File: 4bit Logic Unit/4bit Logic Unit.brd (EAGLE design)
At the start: 161.3 x 110.2 mm, 91 parts

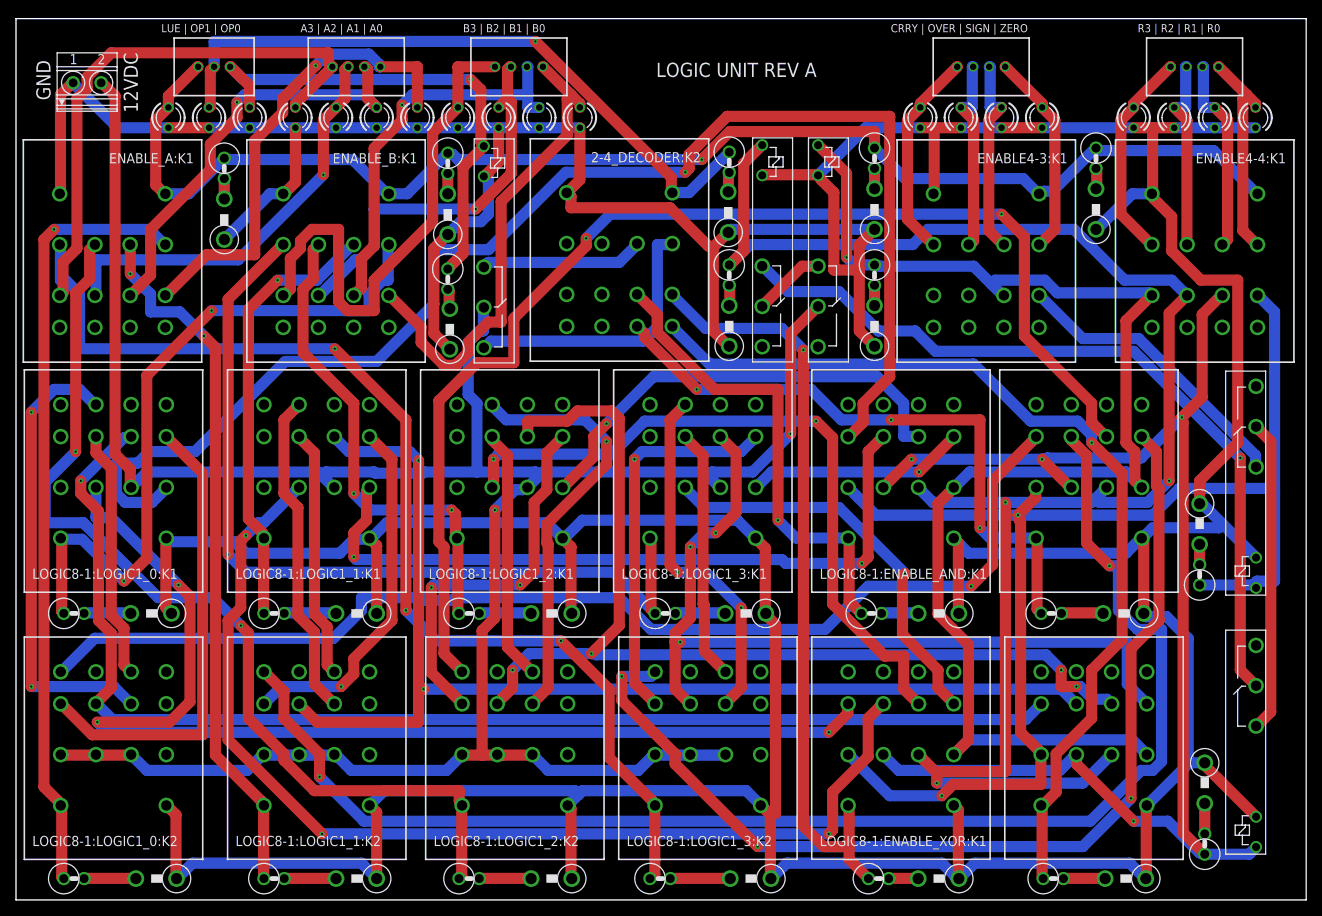
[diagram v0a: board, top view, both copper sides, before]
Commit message: Using updated connectors
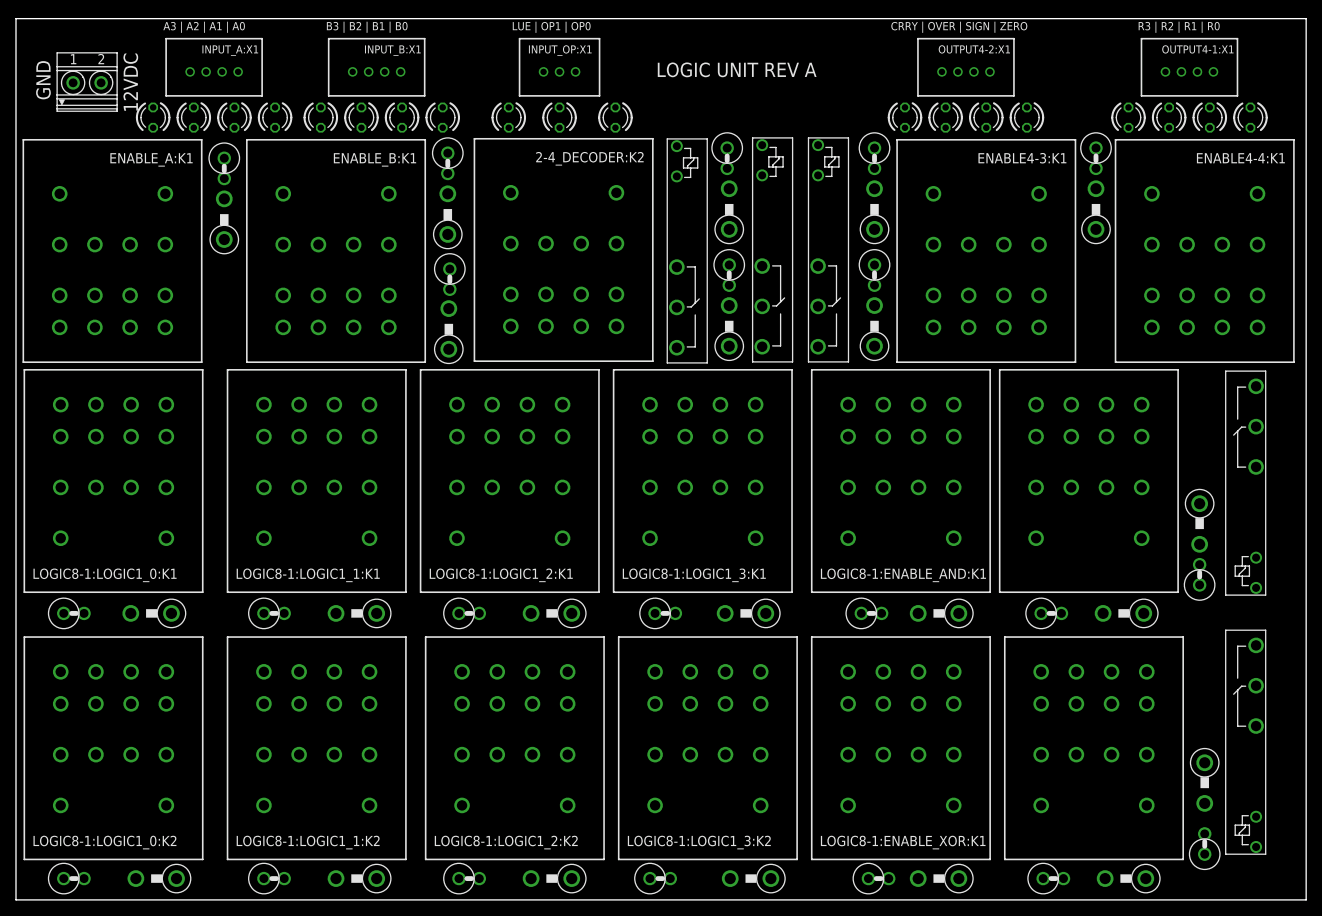
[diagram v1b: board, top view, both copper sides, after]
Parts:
- moved INPUT_OP:LED0 45.7 mm to (74.9, 96.5)
- moved INPUT_OP:LED1 43.8 mm to (67.9, 96.5)
- moved INPUT_OP:X1 43.2 mm to (67.9, 102.2), turned to 180 degrees
- moved INPUT_OP:LED2 42.5 mm to (61.6, 96.5)
- moved 2-4_DECODER:D1 38.1 mm to (88.9, 91.4)
- moved 2-4_DECODER:D2 38.0 mm to (89.2, 85.1)
- moved 2-4_DECODER:D4 37.9 mm to (54.1, 70.1)
- moved 2-4_DECODER:D3 37.9 mm to (54.2, 76.3)
- moved 2-4_DECODER:K1 24.1 mm to (81.4, 93.9)
- moved INPUT_A:X1 17.8 mm to (24.8, 102.2)
- moved INPUT_B:X1 17.8 mm to (45.1, 102.2)
- moved INPUT_A:LED0 17.8 mm to (32.4, 96.5)
- moved INPUT_A:LED1 17.8 mm to (27.3, 96.5)
- moved INPUT_A:LED2 17.8 mm to (22.2, 96.5)
- moved INPUT_A:LED3 17.8 mm to (17.1, 96.5)
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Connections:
- net CARRY: now also OUTPUT4-2:X1.1; no longer OUTPUT4-2:X1.4
- net N$1: now also INPUT_A:X1.4; no longer INPUT_A:X1.1
- net N$2: now also INPUT_A:X1.3; no longer INPUT_A:X1.2
- net N$3: now also INPUT_A:X1.2; no longer INPUT_A:X1.3
- net N$4: now also INPUT_A:X1.1; no longer INPUT_A:X1.4
- net N$5: now also INPUT_B:X1.4; no longer INPUT_B:X1.1
- net N$6: now also INPUT_B:X1.3; no longer INPUT_B:X1.2
- net N$7: now also INPUT_B:X1.2; no longer INPUT_B:X1.3
- net N$8: now also INPUT_B:X1.1; no longer INPUT_B:X1.4
- net OVERFLOW: now also OUTPUT4-2:X1.2; no longer OUTPUT4-2:X1.3
- net R0: now also OUTPUT4-1:X1.4; no longer OUTPUT4-1:X1.1
- net R1: now also OUTPUT4-1:X1.3; no longer OUTPUT4-1:X1.2
- net R2: now also OUTPUT4-1:X1.2; no longer OUTPUT4-1:X1.3
- net R3: now also OUTPUT4-1:X1.1; no longer OUTPUT4-1:X1.4
- net SIGN: now also OUTPUT4-2:X1.3; no longer OUTPUT4-2:X1.2
- net ZERO: now also OUTPUT4-2:X1.4; no longer OUTPUT4-2:X1.1
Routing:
- net GND: track 804.3 -> 0.00 mm
- net +12V: track 309.1 -> 0.00 mm, vias 2 -> 0
- net N$42: track 209.0 -> 0.00 mm, vias 3 -> 0
- net LOGIC8-1:NOT1: track 174.3 -> 0.00 mm, vias 2 -> 0
- net N$41: track 173.6 -> 0.00 mm, vias 4 -> 0
- net LOGIC8-1:AND0: track 173.2 -> 0.00 mm, vias 1 -> 0
- net LUE: track 171.7 -> 0.00 mm, vias 1 -> 0
- net N$43: track 171.7 -> 0.00 mm, vias 1 -> 0
- net N$40: track 168.8 -> 0.00 mm, vias 2 -> 0
- net LOGIC8-1:OR0: track 158.7 -> 0.00 mm, vias 1 -> 0
- net LOGIC8-1:NOT2: track 152.2 -> 0.00 mm, vias 2 -> 0
- net LOGIC8-1:NOT0: track 144.7 -> 0.00 mm, vias 1 -> 0
- net LOGIC8-1:OR1: track 143.4 -> 0.00 mm, vias 2 -> 0
- net LOGIC8-1:XOR0: track 141.9 -> 0.00 mm, vias 3 -> 0
- net N$14: track 138.6 -> 0.00 mm, vias 3 -> 0
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
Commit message: Defining input signals for LU
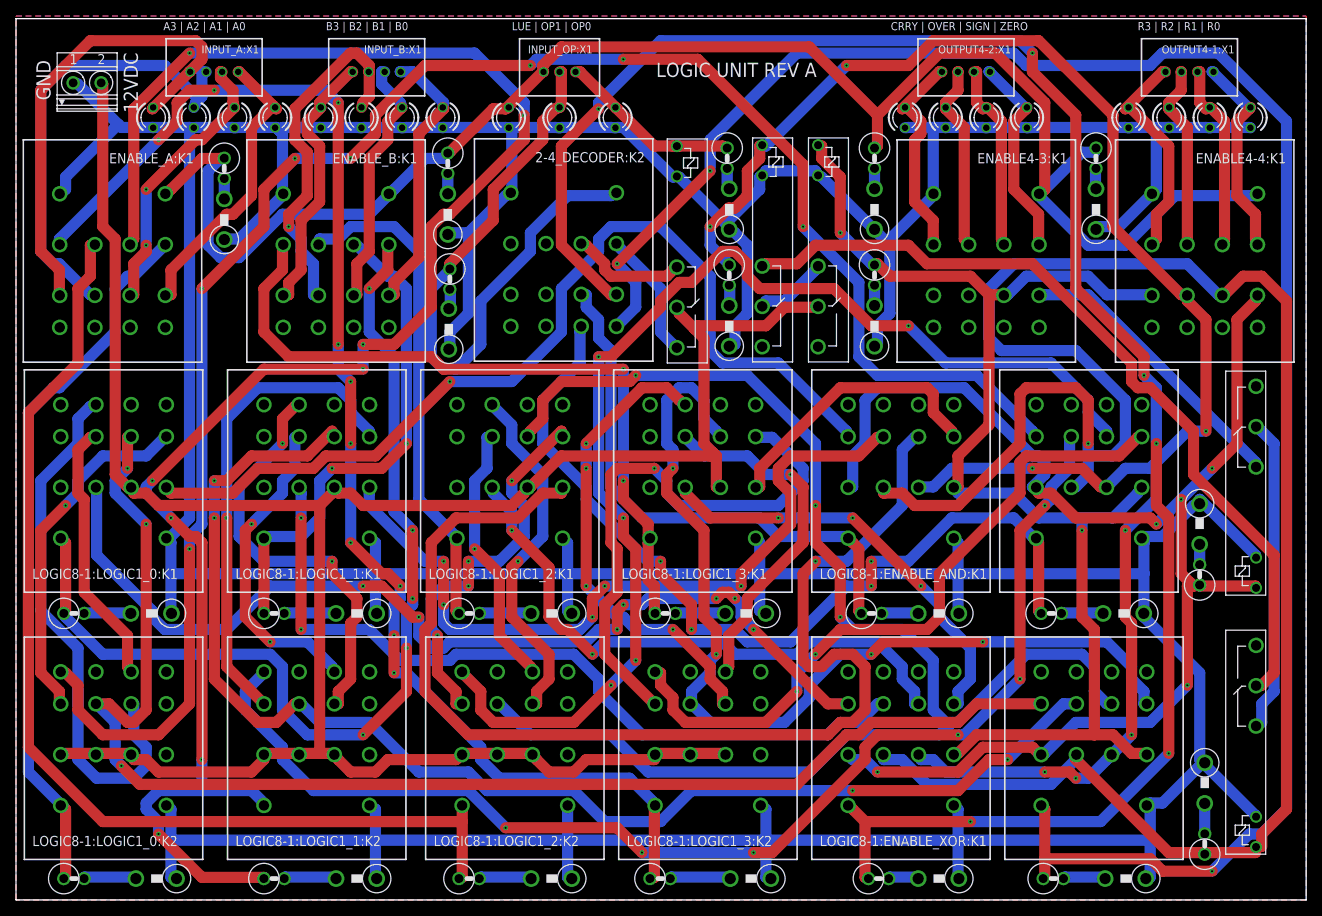
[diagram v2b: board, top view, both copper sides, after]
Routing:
- net GND: track 0.00 -> 763.5 mm
- net +12V: track 0.00 -> 293.6 mm
- net N$41: track 0.00 -> 255.6 mm, vias 0 -> 1
- net N$21: track 0.00 -> 240.9 mm, vias 0 -> 3
- net N$22: track 0.00 -> 233.7 mm, vias 0 -> 6
- net N$16: track 0.00 -> 226.6 mm, vias 0 -> 8
- net LOGIC8-1:NOT0: track 0.00 -> 225.1 mm, vias 0 -> 7
- net N$42: track 0.00 -> 223.8 mm, vias 0 -> 8
- net LUE: track 0.00 -> 206.1 mm
- net LOGIC8-1:OR2: track 0.00 -> 180.8 mm, vias 0 -> 3
- net N$40: track 0.00 -> 175.2 mm, vias 0 -> 5
- net LOGIC8-1:OR0: track 0.00 -> 173.9 mm, vias 0 -> 3
- net N$14: track 0.00 -> 170.6 mm, vias 0 -> 10
- net LOGIC8-1:OR1: track 0.00 -> 166.0 mm, vias 0 -> 4
- net N$43: track 0.00 -> 163.3 mm, vias 0 -> 2
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- added copper zone on layer 1, net +12V
- added copper zone on layer 16, net GND

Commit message: Minor formatting changes
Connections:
- net N$19: now also 2-4_DECODER:K2.44; no longer 2-4_DECODER:K2.32
- net N$22: now also 2-4_DECODER:K2.32; no longer 2-4_DECODER:K2.44
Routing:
- net N$19: track 111.0 -> 110.3 mm
- net N$22: track 233.7 -> 233.0 mm
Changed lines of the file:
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@@
 <?xml version="1.0" encoding="utf-8"?>
 <!DOCTYPE eagle SYSTEM "eagle.dtd">
-<eagle version="8.3.2">
+<eagle version="8.4.3">
 <drawing>
 <settings>
@@
 <param name="dpMaxLengthDifference" value="10mm"/>
 <param name="dpGapFactor" value="2.5"/>
-<param name="checkGrid" value="0"/>
 <param name="checkAngle" value="0"/>
 <param name="checkFont" value="1"/>
 <param name="checkRestrict" value="1"/>
+<param name="checkStop" value="0"/>
 <param name="useDiameter" value="13"/>
 <param name="maxErrors" value="50"/>
@@
 <contactref element="LOGIC8-1:ENABLE_NOT:K1" pad="A2"/>
 <contactref element="LOGIC8-1:ENABLE_NOT:D1" pad="C"/>
-<contactref element="2-4_DECODER:K2" pad="32"/>
 <wire x1="127.8255" y1="43.3832" x2="127.8255" y2="34.8615" width="1.397" layer="1"/>
 <wire x1="127.8255" y1="34.8615" x2="128.143" y2="34.544" width="1.397" layer="1"/>
@@
 <wire x1="124.7267" y1="46.482" x2="116.9797" y2="46.482" width="1.397" layer="16"/>
 <wire x1="127.0508" y1="44.1579" x2="124.7267" y2="46.482" width="1.397" layer="16"/>
-<wire x1="70.4977" y1="69.723" x2="70.653" y2="70.422" width="1.397" layer="16"/>
 <wire x1="127.0508" y1="44.1579" x2="127.512" y2="43.942" width="1.397" layer="16"/>
 <via x="80.5688" y="41.0591" extent="1-16" drill="0.254"/>
@@
 <via x="106.9086" y="37.9603" extent="1-16" drill="0.254"/>
 <via x="106.9086" y="41.0591" extent="1-16" drill="0.254"/>
+<contactref element="2-4_DECODER:K2" pad="44"/>
+<wire x1="70.4977" y1="69.723" x2="75.053" y2="74.422" width="0" layer="19" extent="16-16"/>
 </signal>
 <signal name="N$20">
@@
 <contactref element="LOGIC8-1:ENABLE_XOR:K1" pad="A2"/>
 <contactref element="LOGIC8-1:ENABLE_XOR:D1" pad="C"/>
-<contactref element="2-4_DECODER:K2" pad="44"/>
 <wire x1="106.1339" y1="8.5217" x2="106.1339" y2="1.5494" width="1.397" layer="1"/>
 <wire x1="104.5845" y1="10.0711" x2="106.1339" y2="8.5217" width="1.397" layer="1"/>
@@
 <wire x1="119.3038" y1="8.5217" x2="135.5725" y2="8.5217" width="1.397" layer="16"/>
 <wire x1="106.1339" y1="8.5217" x2="119.3038" y2="8.5217" width="1.397" layer="1"/>
-<wire x1="74.3712" y1="74.3712" x2="75.053" y2="74.422" width="1.397" layer="1"/>
 <via x="72.8218" y="97.6122" extent="1-16" drill="0.254"/>
 <via x="127.0508" y="104.5845" extent="1-16" drill="0.254"/>
@@
 <via x="144.0942" y="17.0434" extent="1-16" drill="0.254"/>
 <via x="119.3038" y="8.5217" extent="1-16" drill="0.254"/>
+<contactref element="2-4_DECODER:K2" pad="32"/>
+<wire x1="74.3712" y1="74.3712" x2="70.653" y2="70.422" width="0" layer="19" extent="1-1"/>
 </signal>
 <signal name="LOGIC8-1:NOT3">
